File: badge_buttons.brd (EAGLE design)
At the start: 82.5 x 58.3 mm, 6 parts

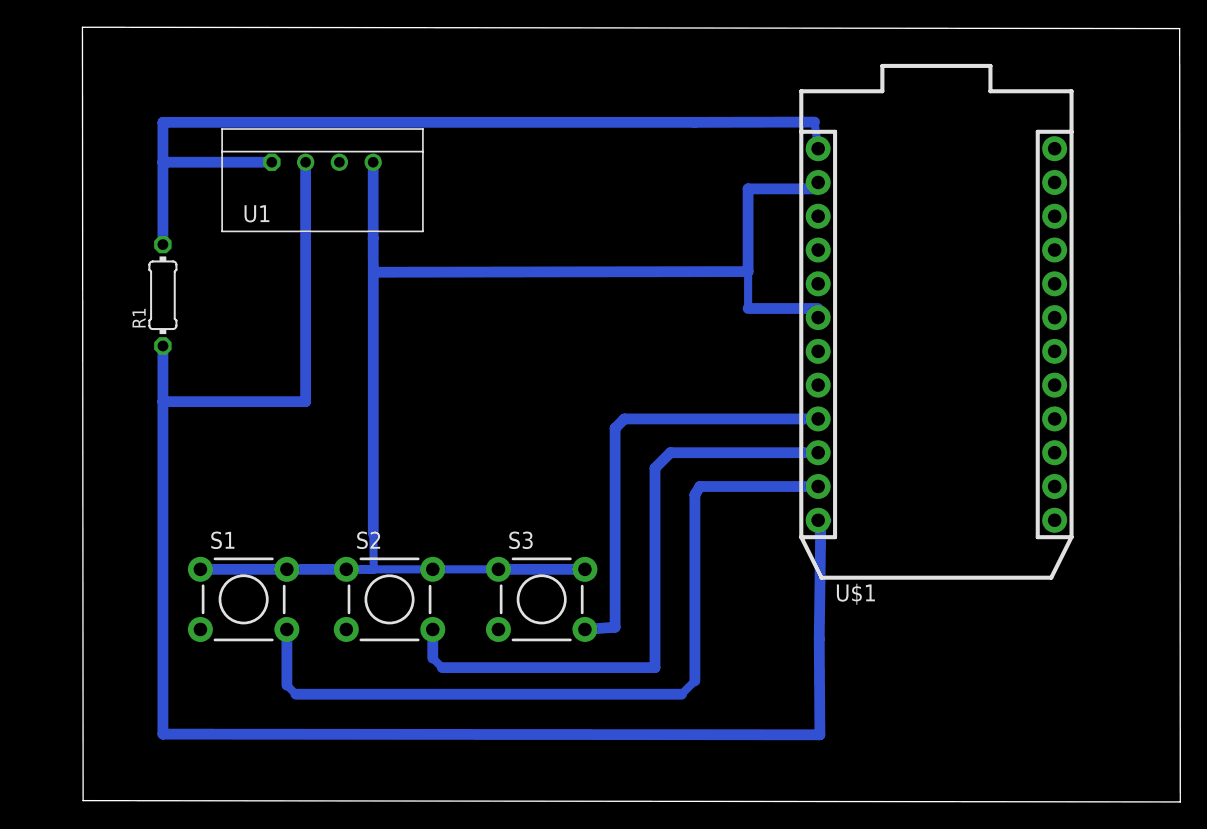
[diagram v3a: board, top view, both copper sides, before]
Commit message: MLX succesfully added to code
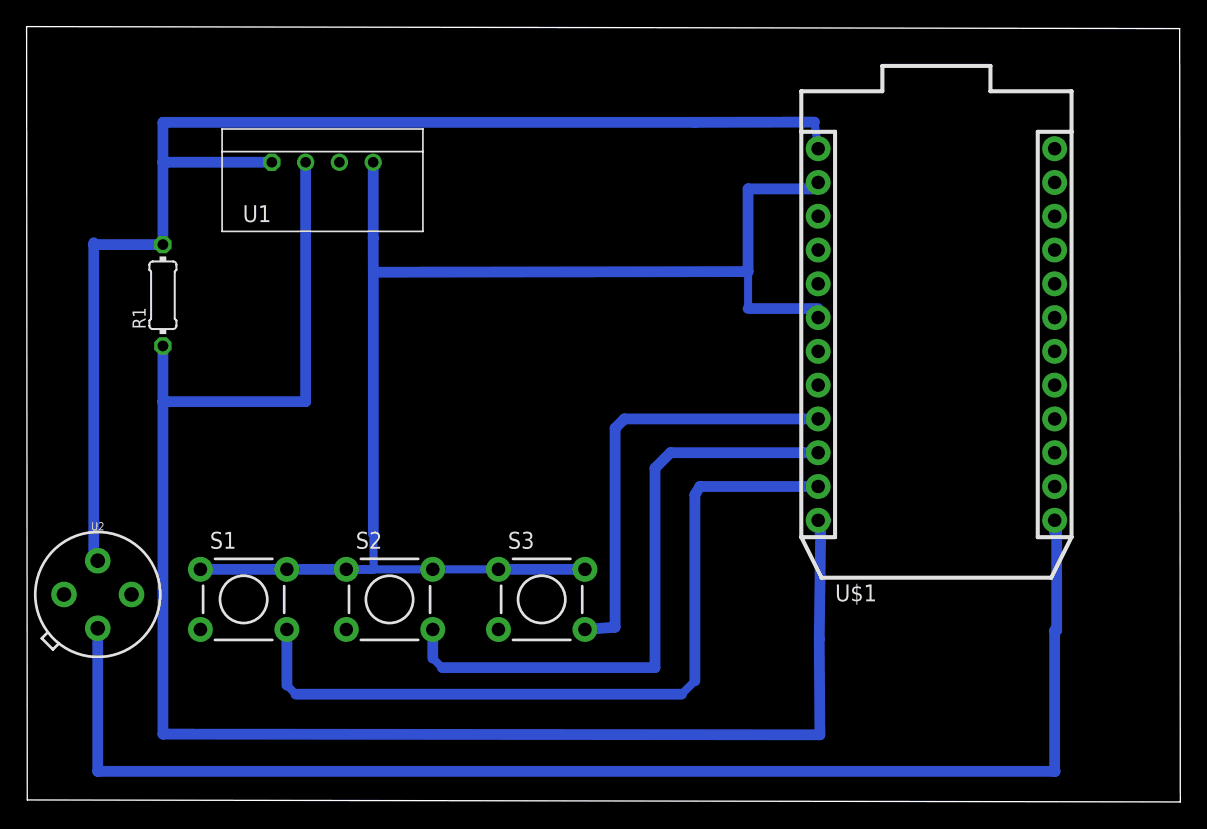
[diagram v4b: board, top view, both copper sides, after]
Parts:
- added U2: MLX90614, SparkFun-Sensors:TO-39
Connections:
- new net N$7: U$1.13, U2.1
- net N$4: now also U2.4
- net N$5: now also U2.3
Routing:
- net N$7: track 0.00 -> 101.9 mm
- net N$5: track 68.4 -> 97.8 mm
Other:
- board size 82.5 x 58.3 mm -> 86.8 x 58.3 mm
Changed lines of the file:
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@@
 <board>
 <plain>
-<wire x1="10" y1="10" x2="92.5" y2="9.9" width="0" layer="20"/>
+<wire x1="5.8" y1="10.05" x2="92.5" y2="9.9" width="0" layer="20"/>
 <wire x1="92.5" y1="9.9" x2="92.45" y2="68.05" width="0" layer="20"/>
-<wire x1="92.45" y1="68.05" x2="9.95" y2="68.15" width="0" layer="20"/>
-<wire x1="9.95" y1="68.15" x2="10" y2="10" width="0" layer="20"/>
+<wire x1="92.45" y1="68.05" x2="5.75" y2="68.2" width="0" layer="20"/>
+<wire x1="5.75" y1="68.2" x2="5.8" y2="10.05" width="0" layer="20"/>
 </plain>
 <attributes>
@@
 </element>
 <element name="R1" library="resistor" library_urn="urn:adsk.eagle:library:348" package="0204/7" package3d_urn="urn:adsk.eagle:package:25945/1" value="" x="16" y="48" rot="R90"/>
+<element name="U2" library="SparkFun-Sensors" package="TO-39" value="MLX90614" x="11.1" y="25.5" rot="R270">
+<attribute name="PROD_ID" value="COMP-09719" x="11.1" y="25.5" size="1.778" layer="27" rot="R270" display="off"/>
+<attribute name="SF_ID" value="SEN-09570" x="11.1" y="25.5" size="1.778" layer="27" rot="R270" display="off"/>
+</element>
 </elements>
 <signals>
@@
 <wire x1="65.27" y1="56" x2="60" y2="56" width="0.8128" layer="16"/>
 <wire x1="60" y1="56" x2="60" y2="49.78" width="0.8128" layer="16"/>
+<contactref element="U2" pad="4"/>
+<wire x1="8.56" y1="25.5" x2="18.8188" y2="27.3906" width="0" layer="19" extent="1-1"/>
 </signal>
 <signal name="N$5">
@@
 <wire x1="65" y1="61.02" x2="65.27" y2="59.02" width="0.6096" layer="16"/>
 <wire x1="16" y1="58" x2="16" y2="51.81" width="0.8128" layer="16"/>
+<contactref element="U2" pad="3"/>
+<wire x1="16" y1="51.81" x2="10.8" y2="51.81" width="0.8128" layer="16"/>
+<wire x1="10.8" y1="51.81" x2="10.8" y2="51.95" width="0.8128" layer="16"/>
+<wire x1="10.8" y1="51.81" x2="10.8" y2="28.04" width="0.8128" layer="16"/>
+<wire x1="10.8" y1="28.04" x2="11.1" y2="28.04" width="0.8128" layer="16"/>
 </signal>
 <signal name="N$6">
@@
 <wire x1="16" y1="44.19" x2="16" y2="40" width="0.8128" layer="16"/>
 </signal>
+<signal name="N$7">
+<contactref element="U2" pad="1"/>
+<contactref element="U$1" pad="13"/>
+<wire x1="11.1" y1="22.96" x2="11.1" y2="12.2" width="0.8128" layer="16"/>
+<wire x1="11.1" y1="12.2" x2="83.05" y2="12.2" width="0.8128" layer="16"/>
+<wire x1="83.1" y1="12.2" x2="83.05" y2="12.2" width="0.8128" layer="16"/>
+<wire x1="83.05" y1="12.2" x2="83.05" y2="22.7996" width="0.8128" layer="16"/>
+<wire x1="83.05" y1="22.7996" x2="83.2024" y2="22.7996" width="0.8128" layer="16"/>
+<wire x1="83.2024" y1="22.7996" x2="83.2024" y2="30.2164" width="0.8128" layer="16"/>
+<wire x1="83.2024" y1="30.2164" x2="83.05" y2="30.2164" width="0.8128" layer="16"/>
+<wire x1="83.05" y1="30.2164" x2="83.05" y2="31.08" width="0.8128" layer="16"/>
+</signal>
 </signals>
